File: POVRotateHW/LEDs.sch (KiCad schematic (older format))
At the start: 14 parts, among them U5 STP08DP05, U6 STP08DP05, U7 STP08DP05

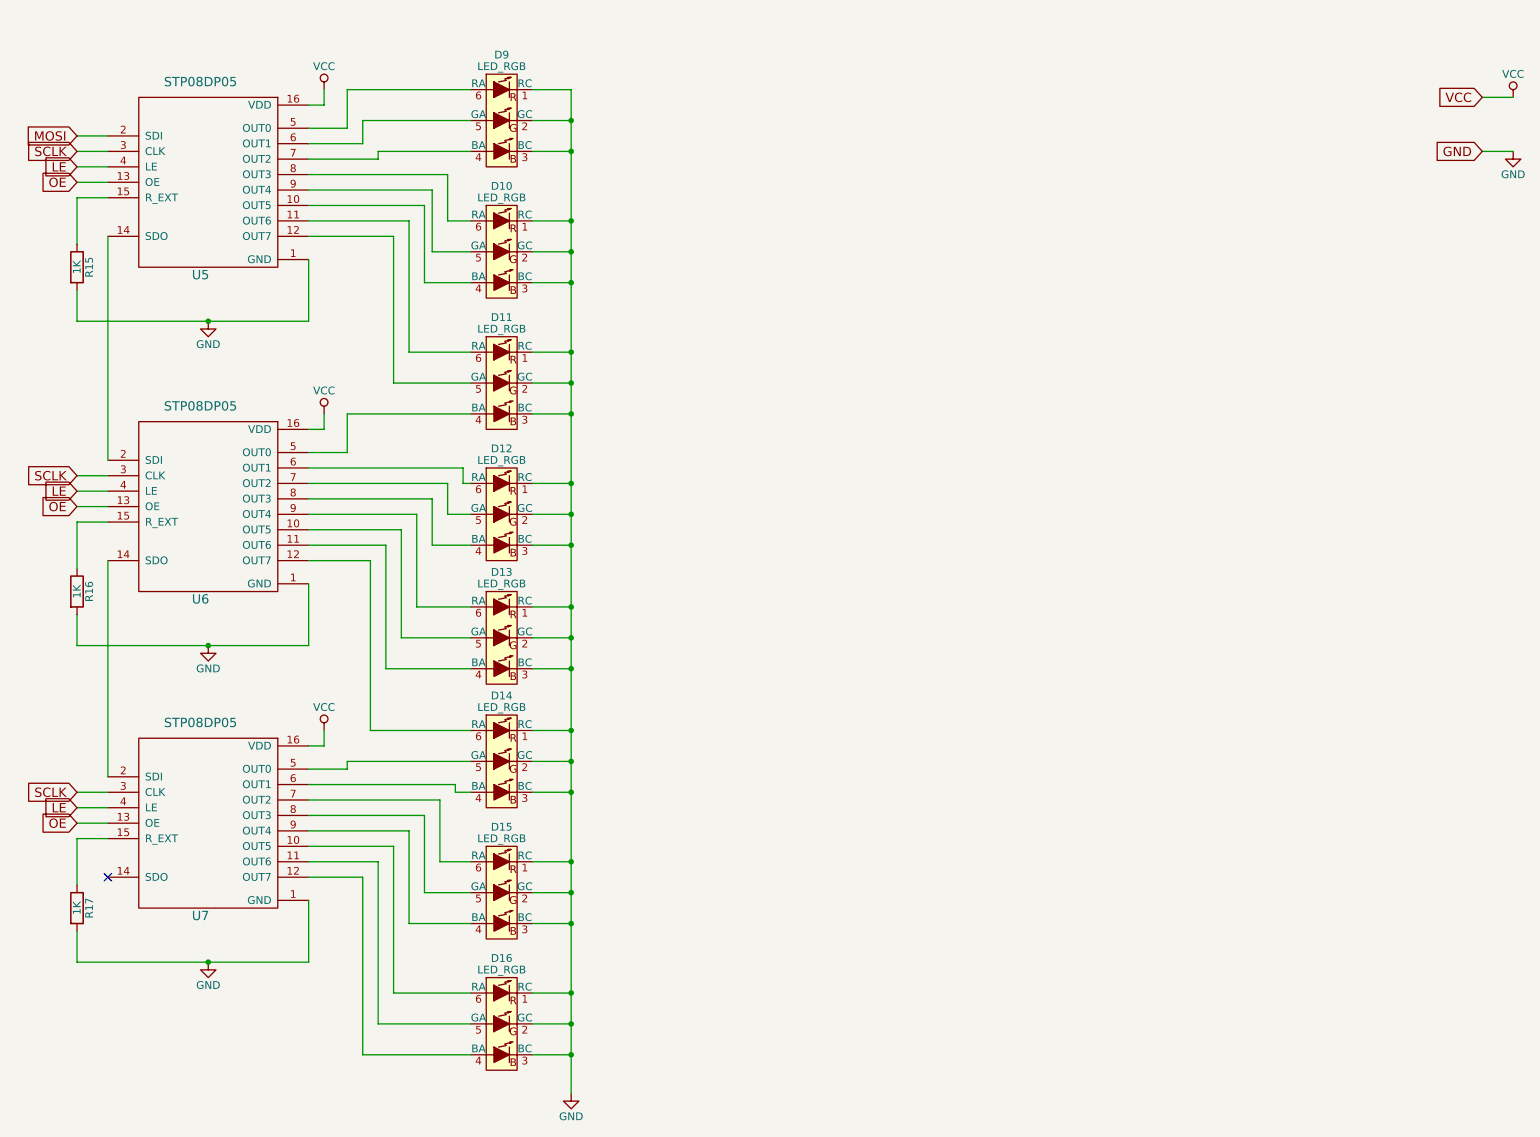
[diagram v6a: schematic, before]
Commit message: Switched the LED driver to a 24-bit LED driver from ST.
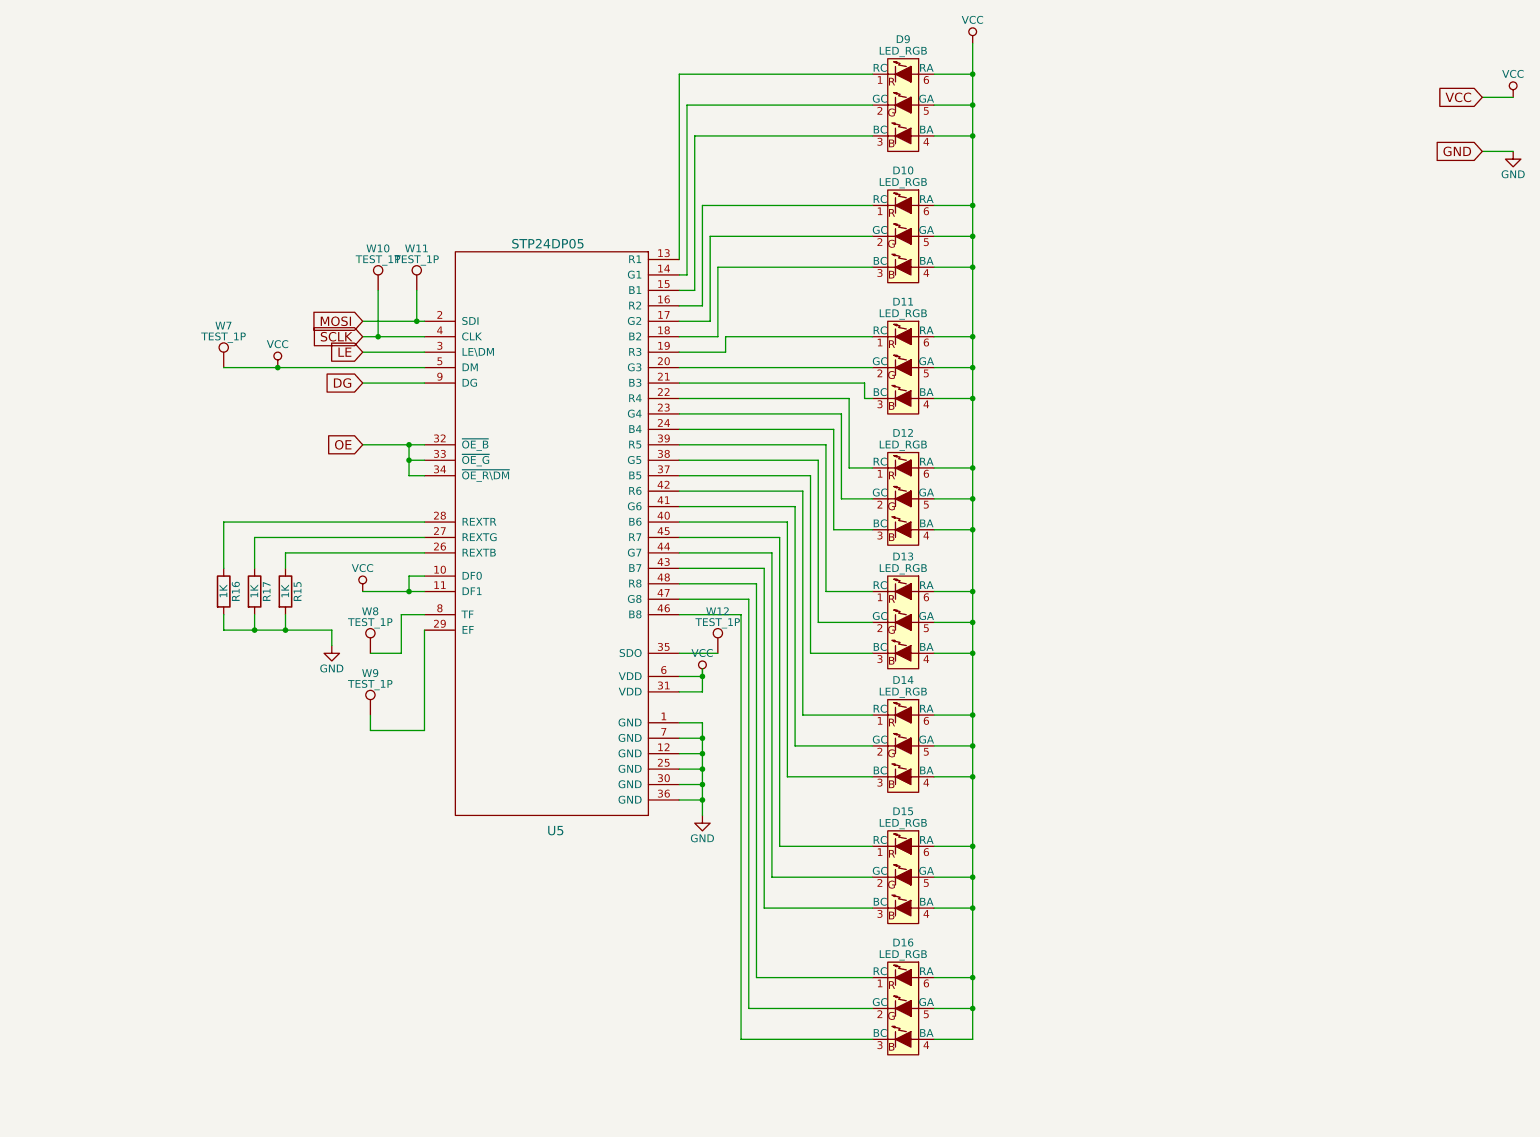
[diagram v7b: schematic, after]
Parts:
- removed U5, U6, U7: STP08DP05, SMD_Packages:SO-16-N, symbol STP08DP05
- added U5: STP24DP05, symbol STP24DP05
- added W10, W11, W12, W7, W8, W9: TEST_1P, symbol TEST_1P
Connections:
- net GND: now also U5.1 (GND), U5.12 (GND), U5.25 (GND), U5.30 (GND), U5.36 (GND), U5.7 (GND); no longer D10.1 (RC), D10.2 (GC), D10.3 (BC), D11.1 (RC), D11.2 (GC), D11.3 (BC), D12.1 (RC), D12.2 (GC), D12.3 (BC), D13.1 (RC), D13.2 (GC), D13.3 (BC), D14.1 (RC), D14.2 (GC), D14.3 (BC), D15.1 (RC), D15.2 (GC), D15.3 (BC), D16.1 (RC), D16.2 (GC), D16.3 (BC), D9.1 (RC), D9.2 (GC), D9.3 (BC)
- net LE: now also U5.3 (LE\DM)
- net MOSI: now also U5.2 (SDI), W11.1
- net OE: now also U5.32 (~OE_B), U5.33 (~OE_G), U5.34 (~OE_R\DM)
- net SCLK: now also U5.4 (CLK), W10.1
- net VCC: now also D10.4 (BA), D10.5 (GA), D10.6 (RA), D11.4 (BA), D11.5 (GA), D11.6 (RA), D12.4 (BA), D12.5 (GA), D12.6 (RA), D13.4 (BA), D13.5 (GA), D13.6 (RA), D14.4 (BA), D14.5 (GA), D14.6 (RA), D15.4 (BA), D15.5 (GA), D15.6 (RA), D16.4 (BA), D16.5 (GA), D16.6 (RA), D9.4 (BA), D9.5 (GA), D9.6 (RA), U5.10 (DF0), U5.11 (DF1), U5.31 (VDD), U5.5 (DM), U5.6 (VDD), W7.1
- net at R15.1: now also U5.26 (REXTB)
- net at R16.1: now also U5.28 (REXTR)
- net at R17.1: now also U5.27 (REXTG)
- new net: D9.1 (RC), U5.13 (R1)
- new net: D9.2 (GC), U5.14 (G1)
- new net: D9.3 (BC), U5.15 (B1)
- new net: D10.1 (RC), U5.16 (R2)
- new net: D10.2 (GC), U5.17 (G2)
- new net: D10.3 (BC), U5.18 (B2)
- new net: D11.1 (RC), U5.19 (R3)
- new net: D11.2 (GC), U5.20 (G3)
- new net: D11.3 (BC), U5.21 (B3)
- new net: D12.1 (RC), U5.22 (R4)
- new net: D12.2 (GC), U5.23 (G4)
- new net: D12.3 (BC), U5.24 (B4)
- new net: D14.1 (RC), U5.42 (R6)
- new net: D14.2 (GC), U5.41 (G6)
- new net: D14.3 (BC), U5.40 (B6)
- new net: D15.1 (RC), U5.45 (R7)
- new net: D15.2 (GC), U5.44 (G7)
- new net: D15.3 (BC), U5.43 (B7)
- new net: D13.1 (RC), U5.39 (R5)
- new net: D13.2 (GC), U5.38 (G5)
- new net: D13.3 (BC), U5.37 (B5)
- new net: D16.1 (RC), U5.48 (R8)
- new net: D16.2 (GC), U5.47 (G8)
- new net: D16.3 (BC), U5.46 (B8)
- new net: U5.29 (EF), W9.1
- new net: U5.35 (SDO), W12.1
- new net: U5.8 (TF), W8.1
- new net DG: U5.9 (DG)
- no-connect marks 1 -> 0
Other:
- moved on the sheet: D10, D11, D12, D13, D14, D15, D16, D9, R15

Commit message: Starting layout on the new design.
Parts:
- removed D10, D11, D12, D13, D14, D15, D16, D9: LED_RGB, LEDs:LED_RGB_PLLC-6, symbol LED_RGB
- added D10, D11, D12, D13, D14, D15, D16, D9: LED_RABG, KicadFootprint:CREE_PLCC4, symbol LED_RABG
- U5: footprint (none) -> Housings_QFP:TQFP-48_7x7mm_Pitch0.5mm
- W10, W11, W12, W7, W8, W9: footprint (none) -> Measurement_Points:Measurement_Point_Round-SMD-Pad_Small
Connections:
- net VCC: now also D10.2 (COMMON_ANODE), D11.2 (COMMON_ANODE), D12.2 (COMMON_ANODE), D13.2 (COMMON_ANODE), D14.2 (COMMON_ANODE), D15.2 (COMMON_ANODE), D16.2 (COMMON_ANODE), D9.2 (COMMON_ANODE)
- net at U5.13 (R1): now also D9.1 (RED_CATHODE)
- net at U5.14 (G1): now also D9.4 (GREEN_CATHODE)
- net at U5.15 (B1): now also D9.3 (BLUE_CATHODE)
- net at U5.16 (R2): now also D10.1 (RED_CATHODE)
- net at U5.17 (G2): now also D10.4 (GREEN_CATHODE)
- net at U5.18 (B2): now also D10.3 (BLUE_CATHODE)
- net at U5.19 (R3): now also D11.1 (RED_CATHODE)
- net at U5.20 (G3): now also D11.4 (GREEN_CATHODE)
- net at U5.21 (B3): now also D11.3 (BLUE_CATHODE)
- net at U5.22 (R4): now also D12.1 (RED_CATHODE)
- net at U5.23 (G4): now also D12.4 (GREEN_CATHODE)
- net at U5.24 (B4): now also D12.3 (BLUE_CATHODE)
- net at U5.42 (R6): now also D14.1 (RED_CATHODE)
- net at U5.41 (G6): now also D14.4 (GREEN_CATHODE)
- net at U5.40 (B6): now also D14.3 (BLUE_CATHODE)
- net at U5.45 (R7): now also D15.1 (RED_CATHODE)
- net at U5.44 (G7): now also D15.4 (GREEN_CATHODE)
- net at U5.43 (B7): now also D15.3 (BLUE_CATHODE)
- net at U5.39 (R5): now also D13.1 (RED_CATHODE)
- net at U5.38 (G5): now also D13.4 (GREEN_CATHODE)
- net at U5.37 (B5): now also D13.3 (BLUE_CATHODE)
- net at U5.48 (R8): now also D16.1 (RED_CATHODE)
- net at U5.47 (G8): now also D16.4 (GREEN_CATHODE)
- net at U5.46 (B8): now also D16.3 (BLUE_CATHODE)
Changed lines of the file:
@@
 Comment4 ""
 $EndDescr
-$Comp
-L LED_RGB D9
-U 1 1 584078E0
-P 6400 1150
-F 0 "D9" H 6400 1575 50  0000 C CNN
-F 1 "LED_RGB" H 6400 1500 50  0000 C CNN
-F 2 "LEDs:LED_RGB_PLLC-6" H 6400 1100 50  0001 C CNN
-F 3 "" H 6400 1100 50  0000 C CNN
-	1    6400 1150
-	1    0    0    -1
-$EndComp
 Text GLabel 10150 1100 0    60   Input ~ 0
 VCC
@@
 $EndComp
 $Comp
-L LED_RGB D10
-U 1 1 58407C6C
-P 6400 2000
-F 0 "D10" H 6400 2425 50  0000 C CNN
-F 1 "LED_RGB" H 6400 2350 50  0000 C CNN
-F 2 "LEDs:LED_RGB_PLLC-6" H 6400 1950 50  0001 C CNN
-F 3 "" H 6400 1950 50  0000 C CNN
-	1    6400 2000
-	1    0    0    -1
-$EndComp
-$Comp
-L LED_RGB D11
-U 1 1 58408176
-P 6400 2850
-F 0 "D11" H 6400 3275 50  0000 C CNN
-F 1 "LED_RGB" H 6400 3200 50  0000 C CNN
-F 2 "LEDs:LED_RGB_PLLC-6" H 6400 2800 50  0001 C CNN
-F 3 "" H 6400 2800 50  0000 C CNN
-	1    6400 2850
-	1    0    0    -1
-$EndComp
-$Comp
-L LED_RGB D12
-U 1 1 5840819E
-P 6400 3700
-F 0 "D12" H 6400 4125 50  0000 C CNN
-F 1 "LED_RGB" H 6400 4050 50  0000 C CNN
-F 2 "LEDs:LED_RGB_PLLC-6" H 6400 3650 50  0001 C CNN
-F 3 "" H 6400 3650 50  0000 C CNN
-	1    6400 3700
-	1    0    0    -1
-$EndComp
-$Comp
-L LED_RGB D14
-U 1 1 58408418
-P 6400 5300
-F 0 "D14" H 6400 5725 50  0000 C CNN
-F 1 "LED_RGB" H 6400 5650 50  0000 C CNN
-F 2 "LEDs:LED_RGB_PLLC-6" H 6400 5250 50  0001 C CNN
-F 3 "" H 6400 5250 50  0000 C CNN
-	1    6400 5300
-	1    0    0    -1
-$EndComp
-$Comp
-L LED_RGB D15
-U 1 1 58408440
-P 6400 6150
-F 0 "D15" H 6400 6575 50  0000 C CNN
-F 1 "LED_RGB" H 6400 6500 50  0000 C CNN
-F 2 "LEDs:LED_RGB_PLLC-6" H 6400 6100 50  0001 C CNN
-F 3 "" H 6400 6100 50  0000 C CNN
-	1    6400 6150
-	1    0    0    -1
-$EndComp
-$Comp
-L LED_RGB D13
-U 1 1 58408B6F
-P 6400 4500
-F 0 "D13" H 6400 4925 50  0000 C CNN
-F 1 "LED_RGB" H 6400 4850 50  0000 C CNN
-F 2 "LEDs:LED_RGB_PLLC-6" H 6400 4450 50  0001 C CNN
-F 3 "" H 6400 4450 50  0000 C CNN
-	1    6400 4500
-	1    0    0    -1
-$EndComp
-$Comp
-L LED_RGB D16
-U 1 1 5840AD18
-P 6400 7000
-F 0 "D16" H 6400 7425 50  0000 C CNN
-F 1 "LED_RGB" H 6400 7350 50  0000 C CNN
-F 2 "LEDs:LED_RGB_PLLC-6" H 6400 6950 50  0001 C CNN
-F 3 "" H 6400 6950 50  0000 C CNN
-	1    6400 7000
-	1    0    0    -1
-$EndComp
-$Comp
 L STP24DP05 U5
 U 1 1 58482E44
@@
 F 0 "U5" H 4150 1550 60  0000 C CNN
 F 1 "STP24DP05" H 4100 5350 60  0000 C CNN
-F 2 "" H 4150 3700 60  0001 C CNN
+F 2 "Housings_QFP:TQFP-48_7x7mm_Pitch0.5mm" H 4150 3700 60  0001 C CNN
 F 3 "" H 4150 3700 60  0001 C CNN
 	1    4150 3700
@@
 $EndComp
 Wire Wire Line
-	6600 950  6850 950
-Wire Wire Line
-	6850 750  6850 7200
-Wire Wire Line
-	6850 1150 6600 1150
-Connection ~ 6850 950
-Wire Wire Line
-	6850 1350 6600 1350
-Connection ~ 6850 1150
-Wire Wire Line
-	6850 1800 6600 1800
-Connection ~ 6850 1350
-Wire Wire Line
-	6850 2000 6600 2000
-Connection ~ 6850 1800
-Wire Wire Line
-	6850 2200 6600 2200
-Connection ~ 6850 2000
-Wire Wire Line
-	6850 2650 6600 2650
-Connection ~ 6850 2200
-Wire Wire Line
-	6850 2850 6600 2850
-Connection ~ 6850 2650
-Wire Wire Line
-	6850 3050 6600 3050
-Connection ~ 6850 2850
-Wire Wire Line
-	6850 3500 6600 3500
-Connection ~ 6850 3050
-Wire Wire Line
-	6850 3700 6600 3700
-Connection ~ 6850 3500
-Wire Wire Line
-	6850 3900 6600 3900
-Connection ~ 6850 3700
-Wire Wire Line
-	6850 4300 6600 4300
-Connection ~ 6850 3900
-Wire Wire Line
-	6850 4500 6600 4500
-Connection ~ 6850 4300
-Wire Wire Line
-	6850 4700 6600 4700
-Connection ~ 6850 4500
-Wire Wire Line
-	6850 5100 6600 5100
-Connection ~ 6850 4700
-Wire Wire Line
-	6850 5300 6600 5300
-Connection ~ 6850 5100
-Wire Wire Line
-	6850 5500 6600 5500
-Connection ~ 6850 5300
-Wire Wire Line
-	6850 5950 6600 5950
-Connection ~ 6850 5500
-Wire Wire Line
-	6850 6150 6600 6150
-Connection ~ 6850 5950
-Wire Wire Line
-	6850 6350 6600 6350
-Connection ~ 6850 6150
-Wire Wire Line
-	6850 6800 6600 6800
-Connection ~ 6850 6350
-Wire Wire Line
-	6850 7000 6600 7000
-Connection ~ 6850 6800
-Wire Wire Line
-	6850 7200 6600 7200
-Connection ~ 6850 7000
-Wire Wire Line
 	6200 950  4950 950
 Wire Wire Line
@@
 F 0 "W8" H 2950 4970 50  0000 C CNN
 F 1 "TEST_1P" H 2950 4900 50  0000 C CNN
-F 2 "" H 3150 4700 50  0000 C CNN
+F 2 "Measurement_Points:Measurement_Point_Round-SMD-Pad_Small" H 3150 4700 50  0001 C CNN
 F 3 "" H 3150 4700 50  0000 C CNN
 	1    2950 4700
@@
 F 0 "W9" H 2950 5370 50  0000 C CNN
 F 1 "TEST_1P" H 2950 5300 50  0000 C CNN
-F 2 "" H 3150 5100 50  0000 C CNN
+F 2 "Measurement_Points:Measurement_Point_Round-SMD-Pad_Small" H 3150 5100 50  0001 C CNN
 F 3 "" H 3150 5100 50  0000 C CNN
 	1    2950 5100
@@
 F 0 "W7" H 2000 3120 50  0000 C CNN
 F 1 "TEST_1P" H 2000 3050 50  0000 C CNN
-F 2 "" H 2200 2850 50  0000 C CNN
+F 2 "Measurement_Points:Measurement_Point_Round-SMD-Pad_Small" H 2200 2850 50  0001 C CNN
 F 3 "" H 2200 2850 50  0000 C CNN
 	1    2000 2850
@@
 F 0 "W12" H 5200 4970 50  0000 C CNN
 F 1 "TEST_1P" H 5200 4900 50  0000 C CNN
-F 2 "" H 5400 4700 50  0000 C CNN
+F 2 "Measurement_Points:Measurement_Point_Round-SMD-Pad_Small" H 5400 4700 50  0001 C CNN
 F 3 "" H 5400 4700 50  0000 C CNN
 	1    5200 4700
@@
 F 0 "W11" H 3250 2620 50  0000 C CNN
 F 1 "TEST_1P" H 3250 2550 50  0000 C CNN
-F 2 "" H 3450 2350 50  0000 C CNN
+F 2 "Measurement_Points:Measurement_Point_Round-SMD-Pad_Small" H 3450 2350 50  0001 C CNN
 F 3 "" H 3450 2350 50  0000 C CNN
 	1    3250 2350
@@
 F 0 "W10" H 3000 2620 50  0000 C CNN
 F 1 "TEST_1P" H 3000 2550 50  0000 C CNN
-F 2 "" H 3200 2350 50  0000 C CNN
+F 2 "Measurement_Points:Measurement_Point_Round-SMD-Pad_Small" H 3200 2350 50  0001 C CNN
 F 3 "" H 3200 2350 50  0000 C CNN
 	1    3000 2350
@@
 	3000 2350 3000 2650
 Connection ~ 3000 2650
+$Comp
+L LED_RABG D9
+U 1 1 58485395
+P 6500 1150
+F 0 "D9" H 6575 1500 50  0000 C CNN
+F 1 "LED_RABG" H 6525 800 50  0000 C CNN
+F 2 "KicadFootprint:CREE_PLCC4" H 6450 1100 50  0001 C CNN
+F 3 "" H 6450 1100 50  0000 C CNN
+	1    6500 1150
+	1    0    0    -1
+$EndComp
+$Comp
+L LED_RABG D10
+U 1 1 58485653
+P 6500 2000
+F 0 "D10" H 6575 2350 50  0000 C CNN
+F 1 "LED_RABG" H 6525 1650 50  0000 C CNN
+F 2 "KicadFootprint:CREE_PLCC4" H 6450 1950 50  0001 C CNN
+F 3 "" H 6450 1950 50  0000 C CNN
+	1    6500 2000
+	1    0    0    -1
+$EndComp
+$Comp
+L LED_RABG D11
+U 1 1 584856FD
+P 6500 2850
+F 0 "D11" H 6575 3200 50  0000 C CNN
+F 1 "LED_RABG" H 6525 2500 50  0000 C CNN
+F 2 "KicadFootprint:CREE_PLCC4" H 6450 2800 50  0001 C CNN
+F 3 "" H 6450 2800 50  0000 C CNN
+	1    6500 2850
+	1    0    0    -1
+$EndComp
+$Comp
+L LED_RABG D12
+U 1 1 58485742
+P 6500 3700
+F 0 "D12" H 6575 4050 50  0000 C CNN
+F 1 "LED_RABG" H 6525 3350 50  0000 C CNN
+F 2 "KicadFootprint:CREE_PLCC4" H 6450 3650 50  0001 C CNN
+F 3 "" H 6450 3650 50  0000 C CNN
+	1    6500 3700
+	1    0    0    -1
+$EndComp
+$Comp
+L LED_RABG D13
+U 1 1 58485796
+P 6500 4500
+F 0 "D13" H 6575 4850 50  0000 C CNN
+F 1 "LED_RABG" H 6525 4150 50  0000 C CNN
+F 2 "KicadFootprint:CREE_PLCC4" H 6450 4450 50  0001 C CNN
+F 3 "" H 6450 4450 50  0000 C CNN
+	1    6500 4500
+	1    0    0    -1
+$EndComp
+$Comp
+L LED_RABG D14
+U 1 1 58485825
+P 6500 5300
+F 0 "D14" H 6575 5650 50  0000 C CNN
+F 1 "LED_RABG" H 6525 4950 50  0000 C CNN
+F 2 "KicadFootprint:CREE_PLCC4" H 6450 5250 50  0001 C CNN
+F 3 "" H 6450 5250 50  0000 C CNN
+	1    6500 5300
+	1    0    0    -1
+$EndComp
+$Comp
+L LED_RABG D15
+U 1 1 58485885
+P 6500 6150
+F 0 "D15" H 6575 6500 50  0000 C CNN
+F 1 "LED_RABG" H 6525 5800 50  0000 C CNN
+F 2 "KicadFootprint:CREE_PLCC4" H 6450 6100 50  0001 C CNN
+F 3 "" H 6450 6100 50  0000 C CNN
+	1    6500 6150
+	1    0    0    -1
+$EndComp
+$Comp
+L LED_RABG D16
+U 1 1 584858F0
+P 6500 7000
+F 0 "D16" H 6575 7350 50  0000 C CNN
+F 1 "LED_RABG" H 6525 6650 50  0000 C CNN
+F 2 "KicadFootprint:CREE_PLCC4" H 6450 6950 50  0001 C CNN
+F 3 "" H 6450 6950 50  0000 C CNN
+	1    6500 7000
+	1    0    0    -1
+$EndComp
+Wire Wire Line
+	6850 750  6850 7000
+Wire Wire Line
+	6850 1150 6800 1150
+Wire Wire Line
+	6850 2000 6800 2000
+Connection ~ 6850 1150
+Wire Wire Line
+	6850 2850 6800 2850
+Connection ~ 6850 2000
+Wire Wire Line
+	6850 3700 6800 3700
+Connection ~ 6850 2850
+Wire Wire Line
+	6850 4500 6800 4500
+Connection ~ 6850 3700
+Wire Wire Line
+	6850 5300 6800 5300
+Connection ~ 6850 4500
+Wire Wire Line
+	6850 6150 6800 6150
+Connection ~ 6850 5300
+Wire Wire Line
+	6850 7000 6800 7000
+Connection ~ 6850 6150
 $EndSCHEMATC
